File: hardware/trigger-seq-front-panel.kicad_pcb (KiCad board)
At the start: 2 copper layers, 91.3 x 128.5 mm, 53 parts

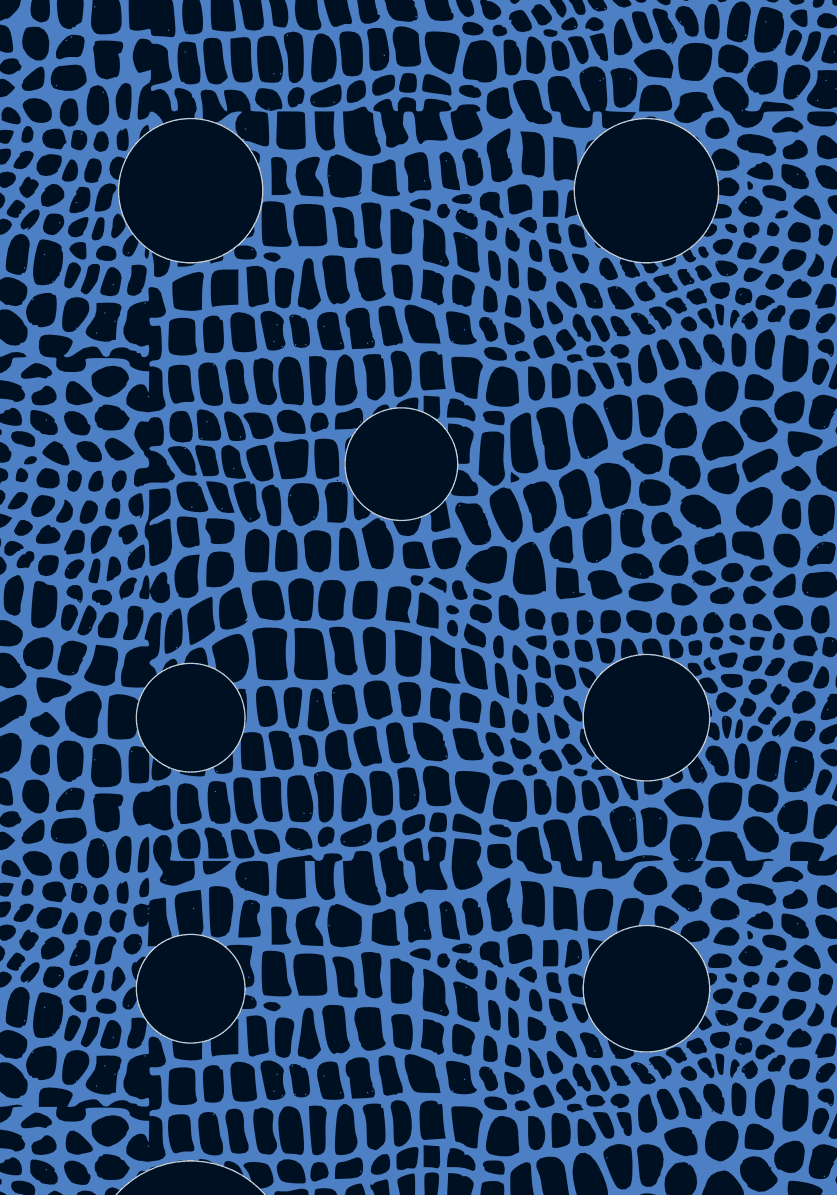
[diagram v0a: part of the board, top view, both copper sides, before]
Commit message: adjusting panel layout (increasing vertical distance of pots, compressing vertical distance of switches, centering 1x16/2x8 switch)
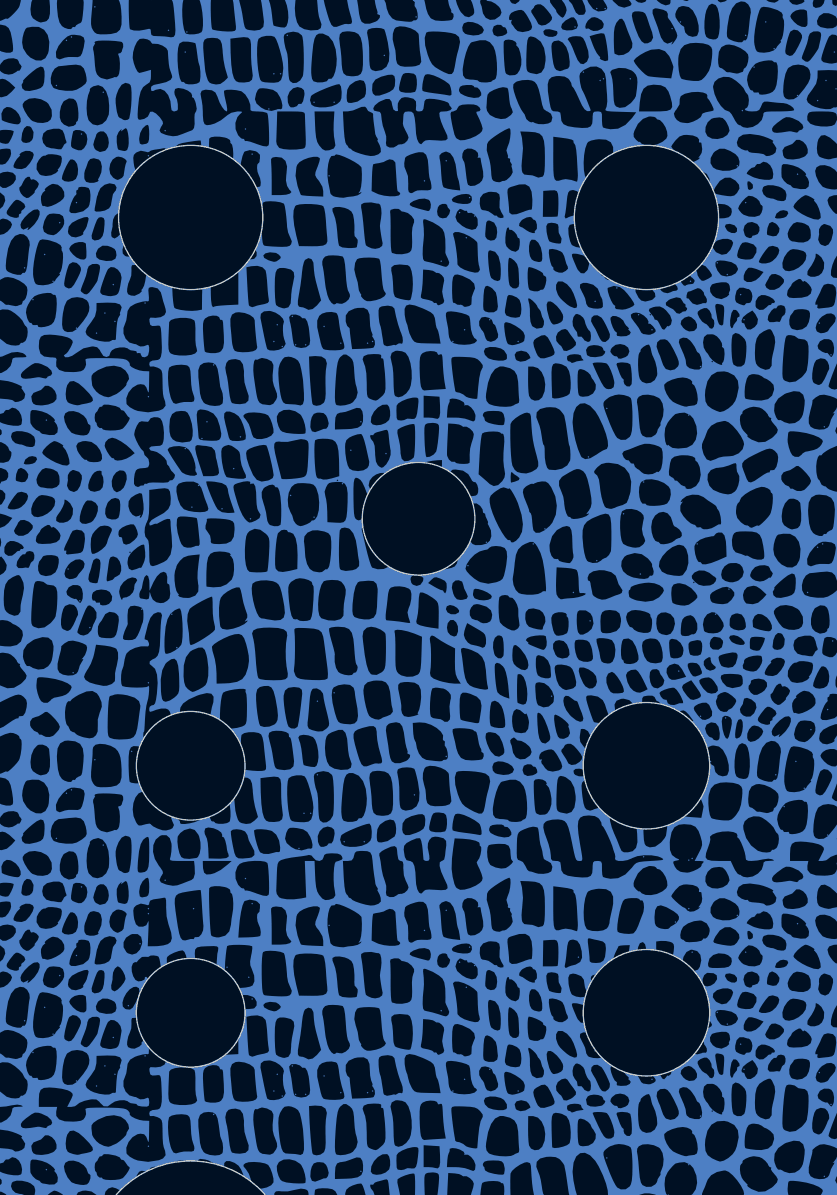
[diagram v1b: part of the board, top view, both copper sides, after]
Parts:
- moved REF** 2.90 mm to (168.2, 87.1)
- moved REF** 2.43 mm to (156.7, 99.6)
- moved REF** 2.43 mm to (179.8, 99.6)
- moved REF** 1.36 mm to (156.7, 71.8)
- moved REF** 1.36 mm to (179.8, 71.8)
- moved REF** 1.22 mm to (156.7, 112.1)
- moved REF** 1.22 mm to (179.8, 112.1)
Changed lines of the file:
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@@
   )
   (footprint "MountingHole:MountingHole_5.5mm" (layer "F.Cu")
-    (at 156.699884 110.869)
+    (at 156.699884 112.085)
     (descr "Mounting Hole 5.5mm, no annular")
     (tags "mounting hole 5.5mm no annular")
@@
   )
   (footprint "MountingHole:MountingHole_5.5mm" (layer "F.Cu")
-    (at 156.699884 97.153)
+    (at 156.699884 99.585)
     (descr "Mounting Hole 5.5mm, no annular")
     (tags "mounting hole 5.5mm no annular")
@@
   )
   (footprint "Mounting_Holes:MountingHole_6.4mm_M6" (layer "F.Cu")
-    (at 179.763953 110.869)
+    (at 179.763953 112.085)
     (descr "Mounting Hole 6.4mm, no annular, M6")
     (tags "mounting hole 6.4mm no annular m6")
@@
   )
   (footprint "Mounting_Holes:MountingHole_6.4mm_M6" (layer "F.Cu")
-    (at 179.763953 97.153)
+    (at 179.763953 99.585)
     (descr "Mounting Hole 6.4mm, no annular, M6")
     (tags "mounting hole 6.4mm no annular m6")
@@
   )
   (footprint "MountingHole:MountingHole_5.5mm" (layer "F.Cu")
-    (at 167.362444 84.322)
+    (at 168.232 87.085)
     (descr "Mounting Hole 5.5mm, no annular")
     (tags "mounting hole 5.5mm no annular")
@@
   )
   (footprint "Mounting_Holes:MountingHole_7.3mm" (layer "F.Cu")
-    (at 156.699884 70.483)
+    (at 156.699884 71.839)
     (descr "Mounting Hole 6.5mm, no annular")
     (tags "mounting hole 6.5mm no annular")
@@
   )
   (footprint "Mounting_Holes:MountingHole_7.3mm" (layer "F.Cu")
-    (at 179.763953 70.483)
+    (at 179.763953 71.839)
     (descr "Mounting Hole 6.5mm, no annular")
     (tags "mounting hole 6.5mm no annular")
@@
   (gr_line (start 190.957 157.474) (end 190.957 29.0135) (layer "Edge.Cuts") (width 0.2))
   (gr_line (start 99.657 29.0135) (end 99.657 157.474) (layer "Edge.Cuts") (width 0.2))
-  (gr_text "run\n" (at 148.879625 92.9894) (layer "B.SilkS")
+  (gr_text "run\n" (at 148.879625 95.4214) (layer "B.SilkS")
     (effects (font (size 1.5 1.5) (thickness 0.3)) (justify mirror))
   )
-  (gr_text "stop\n" (at 148.879625 101.086) (layer "B.SilkS")
+  (gr_text "stop\n" (at 148.879625 103.518) (layer "B.SilkS")
     (effects (font (size 1.5 1.5) (thickness 0.3)) (justify mirror))
   )
-  (gr_text "fwd" (at 149.006625 114.802) (layer "B.SilkS")
+  (gr_text "fwd" (at 149.006625 116.018) (layer "B.SilkS")
     (effects (font (size 1.5 1.5) (thickness 0.3)) (justify mirror))
   )
-  (gr_text "back" (at 149.006625 106.4514) (layer "B.SilkS")
+  (gr_text "back" (at 149.006625 107.6674) (layer "B.SilkS")
     (effects (font (size 1.5 1.5) (thickness 0.3)) (justify mirror))
   )
@@
     (effects (font (size 1.5 1.5) (thickness 0.3)) (justify mirror))
   )
-  (gr_text "steps" (at 179.763953 62.99) (layer "B.SilkS")
+  (gr_text "steps" (at 179.763953 64.346) (layer "B.SilkS")
     (effects (font (size 1.5 1.5) (thickness 0.3)) (justify mirror))
   )
-  (gr_text "swing" (at 156.699884 62.863) (layer "B.SilkS")
+  (gr_text "swing" (at 156.699884 64.219) (layer "B.SilkS")
     (effects (font (size 1.5 1.5) (thickness 0.3)) (justify mirror))
   )
@@
     (effects (font (size 2.54 2.54) (thickness 0.635)) (justify mirror))
   )
-  (gr_text "2x8" (at 167.362444 78.099) (layer "B.SilkS")
+  (gr_text "2x8" (at 168.232 80.862) (layer "B.SilkS")
     (effects (font (size 1.5 1.5) (thickness 0.3)) (justify mirror))
   )
-  (gr_text "1x16" (at 167.362444 90.291) (layer "B.SilkS")
+  (gr_text "1x16" (at 168.232 93.054) (layer "B.SilkS")
     (effects (font (size 1.5 1.5) (thickness 0.3)) (justify mirror))
   )
